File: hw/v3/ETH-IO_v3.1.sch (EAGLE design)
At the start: 82 parts, among them CON1 MC1,5-12-G-3,81, CON2 MC1,5-12-G-3,81, CON3 MC1,5-12-G-3,81, CON4 MC1,5-12-G-3,81, IC1 AP63205, IC2 TLP290-4, IC3 TLP290-4, IC4 TLP290-4, IC5 TLP290-4, IC6 TLP290-4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

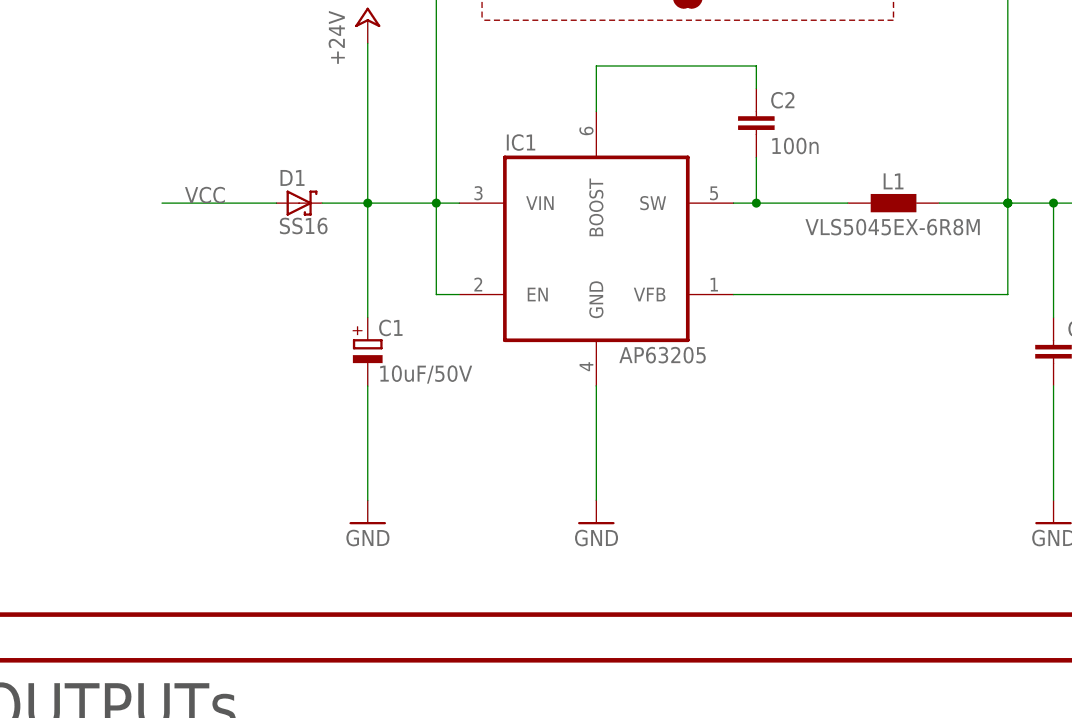
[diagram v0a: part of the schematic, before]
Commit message: bigger footprints
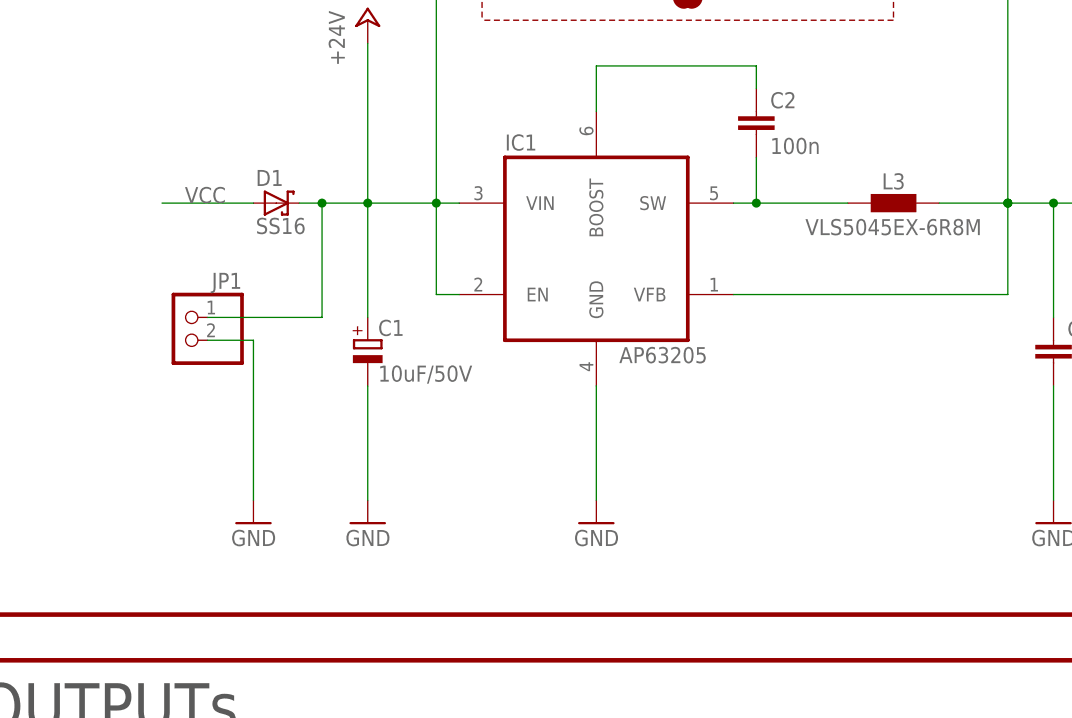
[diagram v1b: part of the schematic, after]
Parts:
- removed L1: VLS5045EX-6R8M, my-inductor:SRN5040-4R7
- added JP1: (no value), pinhead:PINHD-1X2
- added L3: VLS5045EX-6R8M, my-inductor:L5045
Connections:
- net +24V: now also JP1.1
- net +5V: now also L3.1; no longer L1.1
- net GND: now also JP1.2
- net N$67: now also L3.2; no longer L1.2
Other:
- moved on the sheet: D1
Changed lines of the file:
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@@
 <part name="C3" library="rcl" library_urn="urn:adsk.eagle:library:334" deviceset="C-EU" device="C1206" package3d_urn="urn:adsk.eagle:package:23618/2" value="22uF/10V X7R"/>
 <part name="C9" library="rcl" library_urn="urn:adsk.eagle:library:334" deviceset="C-EU" device="C1206" package3d_urn="urn:adsk.eagle:package:23618/2" value="22uF/10V X7R"/>
-<part name="L1" library="my-inductor" deviceset="SRN?-*" device="5040" technology="4R7" value="VLS5045EX-6R8M"/>
 <part name="GND4" library="supply1" library_urn="urn:adsk.eagle:library:371" deviceset="GND" device=""/>
 <part name="R11" library="my-rcl" deviceset="RESISTOR-ARRAY-?" device="1206" package3d_urn="urn:adsk.eagle:package:37264093/1" value="CAY16-392J4LF"/>
@@
 <part name="SJ7" library="jumper" library_urn="urn:adsk.eagle:library:252" deviceset="SJ" device="" package3d_urn="urn:adsk.eagle:package:15471/1"/>
 <part name="LOGO1" library="SparkFun-Aesthetics" deviceset="OSHW-LOGO" device="M-COPPER" value="OSHW-LOGOM-COPPER"/>
+<part name="JP1" library="pinhead" library_urn="urn:adsk.eagle:library:325" deviceset="PINHD-1X2" device="" package3d_urn="urn:adsk.eagle:package:22435/2"/>
+<part name="GND57" library="supply1" deviceset="GND" device=""/>
+<part name="L3" library="my-inductor" deviceset="L?" device="5045" value="VLS5045EX-6R8M"/>
 </parts>
 <sheets>
@@
 <attribute name="VALUE" x="45.72" y="289.56" size="1.778" layer="96" rot="R90"/>
 </instance>
-<instance part="D1" gate="G$1" x="40.64" y="274.32" smashed="yes">
-<attribute name="NAME" x="38.354" y="276.225" size="1.778" layer="95"/>
-<attribute name="VALUE" x="38.354" y="270.891" size="1.778" layer="96"/>
+<instance part="D1" gate="G$1" x="38.1" y="274.32" smashed="yes">
+<attribute name="NAME" x="35.814" y="276.225" size="1.778" layer="95"/>
+<attribute name="VALUE" x="35.814" y="270.891" size="1.778" layer="96"/>
 </instance>
 <instance part="IC3" gate="G$1" x="327.66" y="203.2" smashed="yes">
@@
 <attribute name="VALUE" x="134.239" y="255.524" size="1.27" layer="96" rot="R90" align="top-right"/>
 </instance>
-<instance part="L1" gate="G$1" x="106.68" y="274.32" smashed="yes">
-<attribute name="NAME" x="106.68" y="275.844" size="1.778" layer="95" align="bottom-center"/>
-<attribute name="VALUE" x="106.68" y="272.542" size="1.778" layer="96" align="top-center"/>
-</instance>
 <instance part="GND4" gate="1" x="314.96" y="236.22" smashed="yes">
 <attribute name="VALUE" x="312.42" y="233.68" size="1.778" layer="96"/>
@@
 </instance>
 <instance part="LOGO1" gate="G$1" x="568.96" y="17.78" smashed="yes"/>
+<instance part="JP1" gate="G$1" x="27.94" y="259.08" smashed="yes" rot="MR0">
+<attribute name="NAME" x="34.29" y="264.795" size="1.778" layer="95" rot="MR0"/>
+<attribute name="VALUE" x="34.29" y="254" size="1.778" layer="96" rot="MR0"/>
+</instance>
+<instance part="GND57" gate="1" x="35.56" y="238.76" smashed="yes" rot="MR0">
+<attribute name="VALUE" x="38.1" y="236.22" size="1.778" layer="96" rot="MR0"/>
+</instance>
+<instance part="L3" gate="G$1" x="106.68" y="274.32" smashed="yes">
+<attribute name="NAME" x="106.68" y="275.844" size="1.778" layer="95" align="bottom-center"/>
+<attribute name="VALUE" x="106.68" y="272.542" size="1.778" layer="96" align="top-center"/>
+</instance>
 </instances>
 <busses>
@@
 <wire x1="284.48" y1="127" x2="284.48" y2="124.46" width="0.1524" layer="91"/>
 </segment>
+<segment>
+<pinref part="JP1" gate="G$1" pin="2"/>
+<pinref part="GND57" gate="1" pin="GND"/>
+<wire x1="30.48" y1="259.08" x2="35.56" y2="259.08" width="0.1524" layer="91"/>
+<wire x1="35.56" y1="259.08" x2="35.56" y2="241.3" width="0.1524" layer="91"/>
+</segment>
 </net>
 <net name="N$4" class="0">
@@
 <pinref part="P+10" gate="1" pin="+24V"/>
 <pinref part="D1" gate="G$1" pin="C"/>
+<wire x1="40.64" y1="274.32" x2="43.18" y2="274.32" width="0.1524" layer="91"/>
 <wire x1="43.18" y1="274.32" x2="48.26" y2="274.32" width="0.1524" layer="91"/>
 <wire x1="58.42" y1="274.32" x2="55.88" y2="274.32" width="0.1524" layer="91"/>
@@
 <wire x1="55.88" y1="274.32" x2="55.88" y2="297.18" width="0.1524" layer="91"/>
 <wire x1="55.88" y1="297.18" x2="78.74" y2="297.18" width="0.1524" layer="91"/>
+<pinref part="JP1" gate="G$1" pin="1"/>
+<wire x1="30.48" y1="261.62" x2="43.18" y2="261.62" width="0.1524" layer="91"/>
+<wire x1="43.18" y1="261.62" x2="43.18" y2="274.32" width="0.1524" layer="91"/>
+<junction x="43.18" y="274.32"/>
 </segment>
 <segment>
@@
 <pinref part="C3" gate="G$1" pin="1"/>
 <pinref part="C9" gate="G$1" pin="1"/>
-<pinref part="L1" gate="G$1" pin="1"/>
 <pinref part="SJ7" gate="1" pin="2"/>
 <wire x1="88.9" y1="297.18" x2="119.38" y2="297.18" width="0.1524" layer="91"/>
 <wire x1="119.38" y1="297.18" x2="119.38" y2="274.32" width="0.1524" layer="91"/>
+<pinref part="L3" gate="G$1" pin="1"/>
 </segment>
 <segment>
@@
 <junction x="91.44" y="274.32"/>
 <pinref part="IC1" gate="G$1" pin="SW"/>
-<pinref part="L1" gate="G$1" pin="2"/>
+<pinref part="L3" gate="G$1" pin="2"/>
 </segment>
 </net>
@@
 <segment>
 <pinref part="D1" gate="G$1" pin="A"/>
-<wire x1="38.1" y1="274.32" x2="25.4" y2="274.32" width="0.1524" layer="91"/>
 <label x="27.94" y="274.32" size="1.778" layer="95"/>
-</segment>
-<segment>
+<wire x1="35.56" y1="274.32" x2="25.4" y2="274.32" width="0.1524" layer="91"/>
+</segment>
+<segment>
